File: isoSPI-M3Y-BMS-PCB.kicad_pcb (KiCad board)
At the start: 4 copper layers, 260 x 113 mm, 383 parts, among them J1 Screw_Terminal_01x04, J10 Screw_Terminal_01x04, J11 Screw_Terminal_01x03, J12 Screw_Terminal_01x08, J13 Conn_02x10_Odd_Even, J14 Screw_Terminal_01x04, J15 USB_C_Receptacle_USB2.0_16P, J16 Conn_01x03, J17 USB_C_Receptacle_USB2.0_16P, J18 USB_C_Receptacle_USB2.0_16P, J2 Conn_02x10_Odd_Even, J3 8P8C_LED_Shielded_x2, J5 OEM Shunt Connector, J6 349128020, J7 OEM HV Sense Connector, J8 OEM Connector, J9 Conn_01x03, Q1 CRSM034N06L2, Q2 CRSM034N06L2, Q3 CRSM034N06L2, Q5 CRSM034N06L2, SW1 TS-1187A-B-A-B, SW2 TS-1187A-B-A-B, SW3 TS-1187A-B-A-B, SW4 TS-1187A-B-A-B, U1 SN74LV1T08DBVR, U10 LTV-217-B-G, U11 RP2354B, U12 ADS1115, U13 ISO1050DUB, U15 SN74LV1T08DBVR, U16 BatMan, U17 TPS5430DDAR, U2 ISO1540, U20 LTV-217-B-G, U21 AMS1117-3.3, U22 F0505S-1WR3, U23 SN74LV1T08DBVR, U24 F0505S-1WR3, U25 SN74LV1T08DBVR, U26 SN74LV1T08DBVR, U27 RP2354B, U28 AM26LV32EIDR, U29 B0505S-3WR2, U3 INA228, U30 ISO1540, U32 SP3485EN-L/TR, U4 ISO1540, U6 F0505S-1WR3, U8 LTV-217-B-G, U9 LTV-217-B-G, Y1 ABM8-272-T3, Y2 ABM8-272-T3

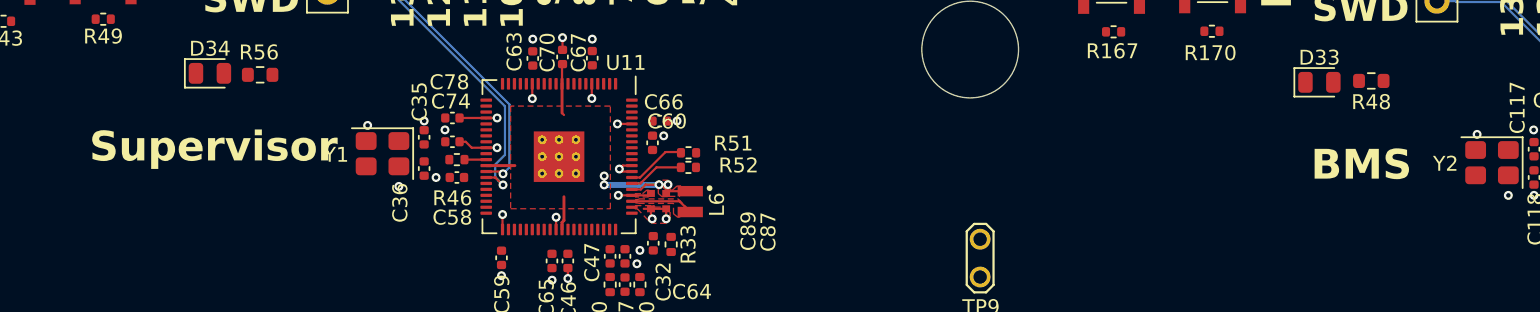
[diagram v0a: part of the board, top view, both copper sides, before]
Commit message: Update isoSPI-M3Y-BMS-PCB.kicad_pcb
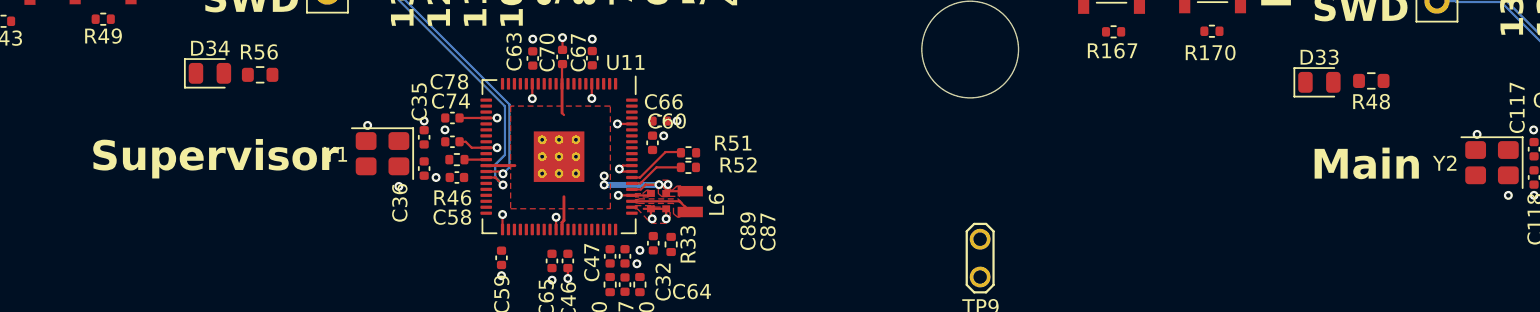
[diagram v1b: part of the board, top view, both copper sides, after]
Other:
- board text added: "Main"
- board text removed: "BMS"
